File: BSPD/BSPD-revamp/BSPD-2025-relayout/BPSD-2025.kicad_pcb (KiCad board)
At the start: 2 copper layers, 72.8 x 55.9 mm, 66 parts, among them J1 SAMMY-3PIN, J2 SAMMY-3PIN, J3 SAMMY-2PIN, J4 SAMMY-5PIN, J5 SAMMY-2PIN, Q1 NMOS, U10 LM397, U11 SN74AHC1G08DBVR, U12 LM397, U17 SN74AHC1G32DBVR, U18 SN74AHC1G32DBVR, U3 LM1117DT-5.0, U4 LM397, U5 LM397, U6 LM397, U7 SN74AHC1G08DBVR, U8 SN74AHC1G00DBVR, U9 LM397

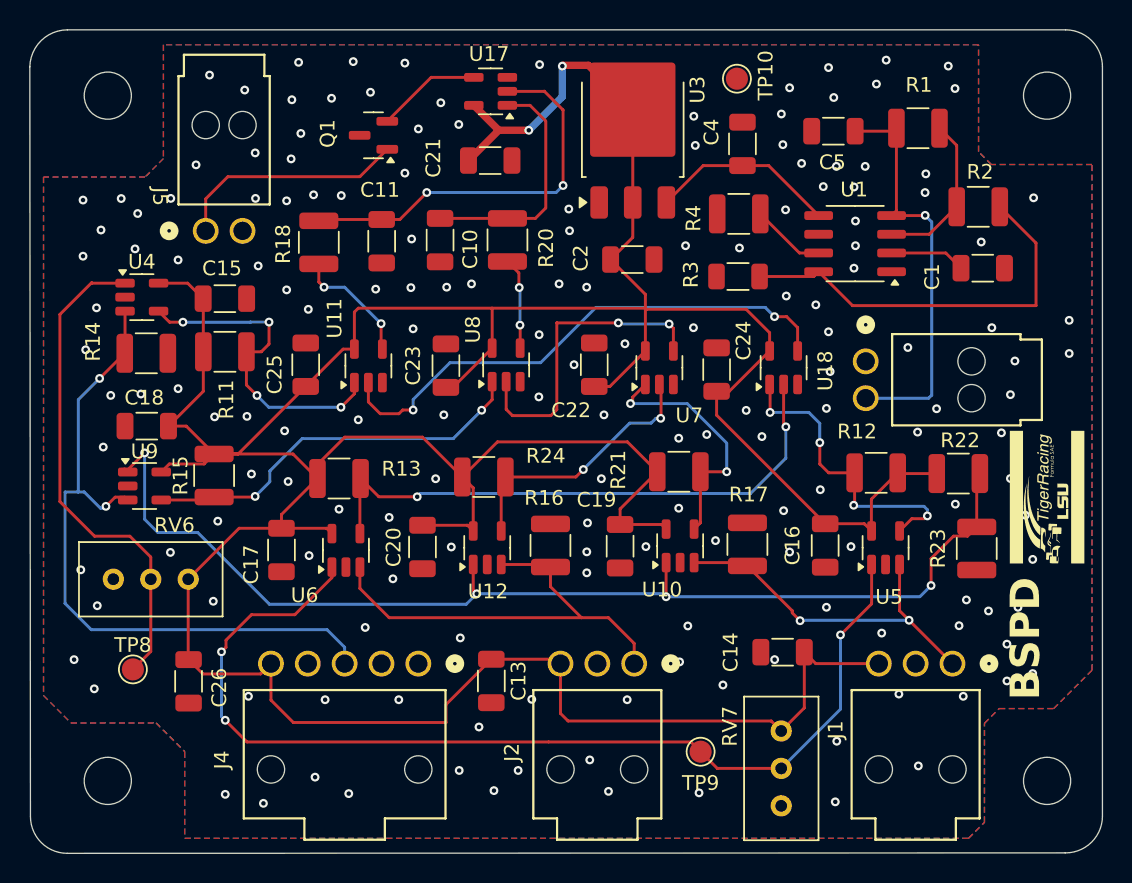
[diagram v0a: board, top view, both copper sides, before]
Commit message: Move output connector to right side and re-connect board
Gerbers and Drills are regenerated, and 3D model is regenerated as well.
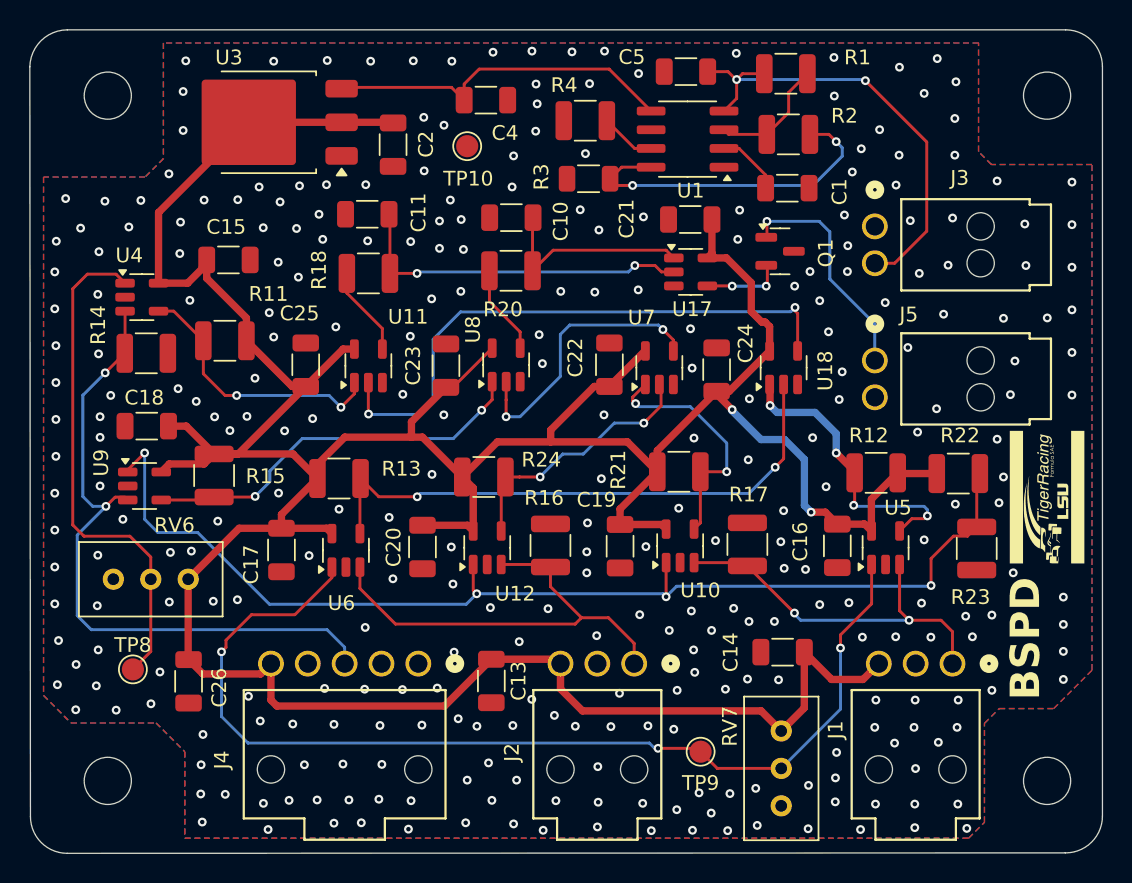
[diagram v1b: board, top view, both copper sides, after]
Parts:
- moved J5 46.3 mm to (155.8, 91.0), turned to 90 degrees
- moved Q1 28.7 mm to (149.4, 83.6), turned to 0 degrees
- moved U3 24.8 mm to (114.6, 74.8), turned to 180 degrees
- moved TP10 18.9 mm to (128.1, 76.4)
- moved U17 18.3 mm to (143.3, 85.0), turned to 0 degrees
- moved C2 18.0 mm to (123.1, 76.3), turned to -90 degrees
- moved C4 17.7 mm to (129.4, 73.3), turned to 0 degrees
- moved C1 14.3 mm to (149.9, 79.3)
- moved C21 14.2 mm to (143.3, 81.4), turned to 0 degrees
- moved R2 13.8 mm to (149.9, 75.6)
- moved U1 13.4 mm to (143.1, 76.0)
- moved R4 12.2 mm to (136.2, 74.7)
- moved R3 12.1 mm to (136.4, 78.6)
- moved C5 10.8 mm to (143.0, 71.4)
- moved R1 9.70 mm to (149.8, 71.5)
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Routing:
- net +5V: track 271.1 -> 255.3 mm
- net Net-(U1-OUT): track 12.8 -> 24.0 mm
- net Net-(U1-OVP): track 27.6 -> 22.4 mm, vias 0 -> 2
- net Net-(R11-Pad1): track 22.4 -> 18.4 mm, vias 4 -> 2
- net +12V: track 27.9 -> 31.9 mm, vias 1 -> 2
- net Net-(C11-Pad1): track 26.9 -> 23.6 mm
- net Net-(U11-Pad2): track 36.3 -> 39.5 mm
- net Net-(U1-ENUV): track 11.0 -> 8.29 mm
- net Net-(C10-Pad1): track 16.4 -> 14.0 mm
- net /BRAKE+CURRENT_HOLD: track 8.27 -> 6.14 mm, vias 2 -> 0
- net /ACCUM_V: track 47.5 -> 45.5 mm
- net Net-(U7-Pad4): track 21.1 -> 19.1 mm
- net Net-(Q1-G): track 7.11 -> 5.37 mm, vias 0 -> 2
- net Net-(U1-ILM): track 5.06 -> 3.78 mm
- net /BSE_1: track 24.2 -> 25.4 mm
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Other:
- board text added: "J3"

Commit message: Reroute BSPD and adjust connector spacing
The other routing was atrocious. Also regenerated gerbers, drills, and 3d model.
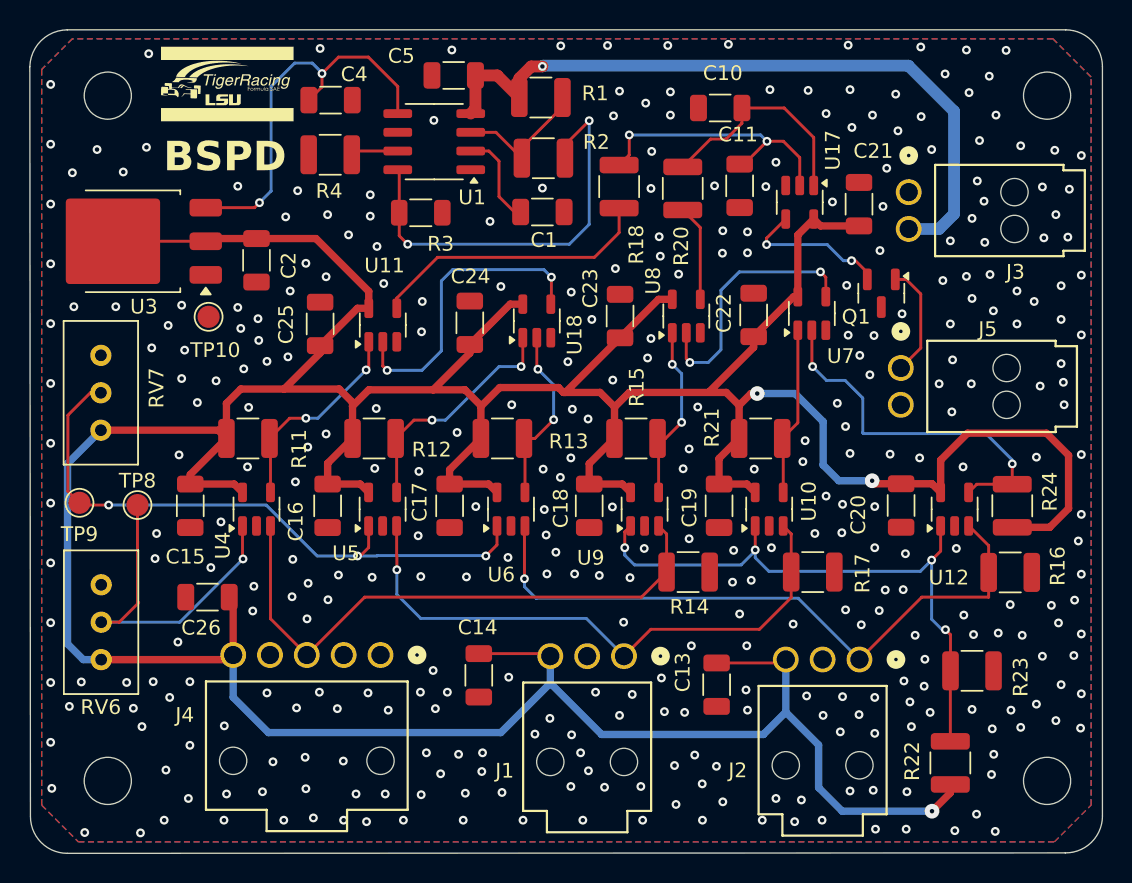
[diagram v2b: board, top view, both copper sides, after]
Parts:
- moved G*** 62.3 mm to (111.9, 72.2), turned to 0 degrees
- moved RV7 50.5 mm to (103.3, 95.7), turned to -90 degrees
- moved TP9 45.4 mm to (101.8, 100.6)
- moved R14 39.7 mm to (143.1, 105.3)
- moved R24 35.9 mm to (165.1, 100.8), turned to -90 degrees
- moved C16 34.7 mm to (118.7, 100.8)
- moved U5 34.2 mm to (122.4, 101.1)
- moved R12 34.2 mm to (121.8, 96.3), turned to 180 degrees
- moved U9 34.0 mm to (140.2, 101.1), turned to 90 degrees
- moved C20 32.6 mm to (157.6, 100.8)
- moved U12 31.8 mm to (161.2, 101.1)
- moved R16 31.3 mm to (165.0, 105.4), turned to 180 degrees
- moved C18 30.5 mm to (136.4, 100.8), turned to 90 degrees
- moved R15 28.7 mm to (139.6, 96.3), turned to 180 degrees
- moved C11 25.3 mm to (146.6, 79.1), turned to -90 degrees
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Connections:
- C5 pad 2: GNDPWR -> GND
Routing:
- net +5V: track 255.3 -> 304.3 mm, vias 2 -> 3
- net /0.455V: track 76.2 -> 42.1 mm
- net /THRESH_BSE: track 70.8 -> 42.8 mm
- net Net-(R13-Pad1): track 39.1 -> 12.2 mm
- net Net-(U11-Pad2): track 39.5 -> 20.8 mm
- net +12V: track 31.9 -> 49.2 mm, vias 2 -> 1
- net Net-(R15-Pad1): track 26.6 -> 12.0 mm
- net /BSE_1: track 25.4 -> 39.9 mm, vias 2 -> 1
- net /BSE_2: track 30.6 -> 44.8 mm, vias 0 -> 1
- net /BRAKE+CURRENT_HOLD: track 6.14 -> 19.3 mm
- net /THRESH_ACCUM: track 34.6 -> 23.4 mm, vias 0 -> 1
- net BSPD_OUT: track 15.6 -> 7.72 mm, vias 1 -> 0
- net Net-(R24-Pad1): track 17.3 -> 24.9 mm
- net /ACCUM_V: track 45.5 -> 39.7 mm, vias 2 -> 0
- net Net-(R21-Pad1): track 16.9 -> 11.4 mm, vias 2 -> 0
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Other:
- board text removed: "Also, in case I forget, Yianni the connector footprints are in your Downloads folder and we can't reimport them if we accidentally delete them! Please put them in the actual project!"
- board text removed: "DRC says front and back ground zones are disconnected. If anyone can figure out where that would be cool (I can't)."
- board text removed: "NOTE! USING GND AND GNDPWR MESSES UP PCB LAYOUT. GNDPWR IS UNCONNECTED. (FOR YIANNI)"

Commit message: Connectors, time delay, vreferences
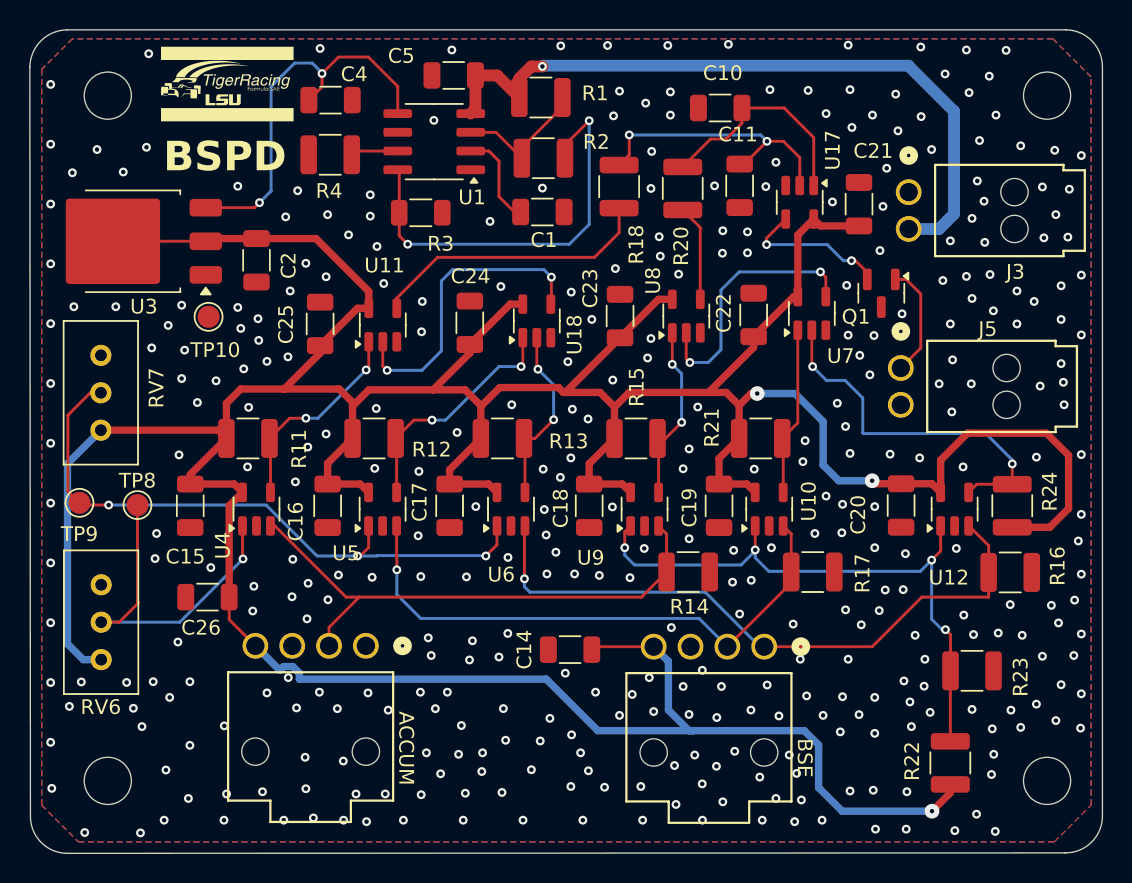
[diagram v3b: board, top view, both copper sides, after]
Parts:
- removed C13: 0.1uF, Capacitor_SMD:C_1206_3216Metric
- removed J1, J2: SAMMY-3PIN, BSPD:SAMMY-3PIN
- removed J4: SAMMY-5PIN, BSPD:SAMMY-5PIN
- added ACCUM: SAMMY-4PIN, BSPD:SAMMY-4PIN, F.Cu at (121.3, 110.3)
- added BSE: SAMMY-4PIN, BSPD:SAMMY-4PIN, F.Cu at (148.3, 110.4)
- R18: value 2.2k -> 4k87
- R22: value 10k -> 12k
- moved C14 6.44 mm to (135.1, 110.6), turned to 180 degrees
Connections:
- net /0.455V renamed /0.385V
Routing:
- net +5V: track 304.3 -> 294.0 mm
- net /ACCUM_V: track 39.7 -> 36.9 mm
- net /BSE_1: track 39.9 -> 38.8 mm
- net /BSE_2: track 44.8 -> 44.1 mm
- net GND: vias 353 -> 370
